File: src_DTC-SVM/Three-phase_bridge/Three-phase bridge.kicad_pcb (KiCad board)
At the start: 2 copper layers, 588 x 429.8 mm, 79 parts, among them K1 CONN_3, M1 MCP6022-I/P, M2 MCP6022-I/P, P1 CONN_1, P2 Fuse, P3 CONN_1, P4 CONN_1, P5 CONN_1, P6 CONN_2, SW1 SW_PUSH_SMALL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

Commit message: Kicad pcb has been separated into three bloks: stm32 connections, three-phase bridge and current sensing. The idea is to have the current operational and diffential amplifiers as close as possible to the shunt resistors and the stm32 pins so that there are no electromagnetic interferencies nor logs to the distance, specially because they are analog signals.
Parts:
- removed SW1, SW2, SW3, SW4, SW5, SW6: SW_PUSH_SMALL, SW_PUSH_SMALL
- moved STM32_CONN1 83.8 mm to (155.2, 56.4)
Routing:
- net VDD: track 205.6 -> 104.8 mm
- net N-0000029: track 12.6 -> 85.6 mm, vias 0 -> 1
- net N-0000031: track 0.00 -> 61.5 mm
- net N-000008: track 0.00 -> 61.3 mm
- net GND: track 432.6 -> 394.1 mm
- net N-000007: track 17.6 -> 28.2 mm, vias 0 -> 1
- net N-000005: track 16.9 -> 15.9 mm

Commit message: Updating the three parts of the pcb.
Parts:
- moved BT1 241.7 mm to (148.8, 124.0)
- moved BT2 241.7 mm to (148.8, 144.0)
- moved D1 241.7 mm to (144.3, 83.8)
- moved INA1 241.7 mm to (126.2, 46.7)
- moved INA2 241.7 mm to (126.0, 93.5)
- moved M1 241.7 mm to (126.0, 64.3)
- moved M2 241.7 mm to (128.5, 118.0)
- moved P2 241.7 mm to (143.8, 117.9)
- moved P6 241.7 mm to (148.8, 134.1)
- moved R10 241.7 mm to (119.6, 124.2)
- moved R6 241.7 mm to (124.7, 131.8)
- moved R8 241.7 mm to (119.6, 70.9)
- moved R9 241.7 mm to (134.6, 54.9)
- moved R_Shunt_2 241.7 mm to (117.3, 115.1)
- moved R11 241.7 mm to (129.8, 73.7)
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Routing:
- net GND: track 394.1 -> 328.2 mm

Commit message: Schematic and PCB updated.
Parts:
- added C10: 0.1uF, 6mm_C, F.Cu at (277.4, 105.4)
- added C11: 0.33uF, 6mm_C, F.Cu at (262.9, 108.0)
- added C12: 1000uF, 10mm_C, F.Cu at (411.0, 58.2)
- added C13: 1000uF, 10mm_C, F.Cu at (414.8, 79.8)
- added C14: 100uF, 6mm_C, F.Cu at (414.8, 88.9)
- added C15: 100uF, 6mm_C, F.Cu at (411.0, 67.8)
- added C8: 0.1uF, 6mm_C, F.Cu at (277.6, 18.0)
- added C9: 2.2uF, 6mm_C, F.Cu at (285.0, 15.5)
- C1, C2: footprint C1 -> 10mm_C
- C3, C4, C5, C6, C7: footprint C1 -> 6mm_C
- moved STM32_CONN1 189.4 mm to (210.1, 132.8)
- moved D1 185.0 mm to (329.2, 88.4)
- moved BT1 185.0 mm to (333.8, 128.5)
- moved BT2 185.0 mm to (333.8, 148.6)
- moved P2 185.0 mm to (328.7, 122.4)
- moved P6 185.0 mm to (333.8, 138.7)
- moved R_Shunt_2 161.0 mm to (273.1, 74.2), turned to 180 degrees
- moved R_Shunt_1 158.5 mm to (274.1, 42.2), turned to 180 degrees
- moved M2 105.1 mm to (230.0, 90.4)
- moved R10 105.1 mm to (221.1, 96.6)
- moved R12 105.1 mm to (223.6, 84.2)
- moved R6 101.5 mm to (221.1, 99.9), turned to 0 degrees
- moved R7 99.2 mm to (223.6, 80.9), turned to 0 degrees
- moved INA2 84.2 mm to (208.7, 77.6), turned to 180 degrees
- moved R9 79.7 mm to (208.9, 83.7)
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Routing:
- net N-0000064: track 144.1 -> 0.00 mm, vias 1 -> 0
- net +48V: track 25.5 -> 124.4 mm
- net GND: track 328.2 -> 421.1 mm
- net N-0000066: track 108.3 -> 20.9 mm
- net N-0000063: track 109.7 -> 23.9 mm, vias 1 -> 0
- net VCC: track 80.4 -> 161.1 mm
- net N-0000065: track 95.6 -> 20.5 mm
- net N-0000010: track 85.6 -> 12.2 mm, vias 1 -> 0
- net N-0000097: track 6.14 -> 71.1 mm, vias 0 -> 1
- net N-0000060: track 83.3 -> 19.8 mm
- net N-0000094: track 0.00 -> 59.2 mm
- net N-0000079: track 61.3 -> 2.54 mm
- net N-0000093: track 0.00 -> 55.1 mm
- net N-000007: track 61.5 -> 13.0 mm
- net N-0000068: track 54.1 -> 100.6 mm, vias 0 -> 1
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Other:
- board outline removed

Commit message: The two INA148 have been wired.
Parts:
- moved P5 123.2 mm to (342.9, 134.4)
- moved P4 93.6 mm to (241.3, 74.2)
- moved P1 86.8 mm to (248.4, 42.2)
- moved R6 68.0 mm to (214.4, 32.3), turned to 270 degrees
- moved R10 64.5 mm to (217.7, 32.3), turned to 270 degrees
- moved C14 62.9 mm to (360.7, 120.9)
- moved C13 62.7 mm to (360.7, 111.5)
- moved C12 60.9 mm to (360.7, 92.5)
- moved C15 60.9 mm to (360.7, 102.1)
- moved R12 49.8 mm to (230.1, 34.8), turned to 90 degrees
- moved M2 49.7 mm to (223.9, 41.1), turned to 90 degrees
- moved R7 47.1 mm to (233.4, 34.8), turned to 270 degrees
- moved INA1 45.4 mm to (236.0, 50.3), turned to 90 degrees
- moved R5 38.3 mm to (232.4, 71.9), turned to 270 degrees
- moved R8 37.8 mm to (218.7, 69.3), turned to 270 degrees
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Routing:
- net +3.3V: track 37.9 -> 166.0 mm, vias 2 -> 1
- net N-0000077: track 61.5 -> 120.8 mm
- net GND: track 421.1 -> 479.2 mm, vias 0 -> 2
- net N-0000097: track 71.1 -> 27.3 mm, vias 1 -> 0
- net N-00000101: track 17.3 -> 58.7 mm, vias 0 -> 1
- net VDD: track 105.9 -> 136.8 mm
- net N-0000010: track 12.2 -> 39.4 mm
- net N-0000075: track 6.78 -> 31.3 mm, vias 0 -> 1
- net N-0000084: track 89.7 -> 112.2 mm
- net N-000007: track 13.0 -> 27.6 mm
- net (no net): track 13.7 -> 0.00 mm
- net N-0000081: track 0.00 -> 10.8 mm
- net N-0000068: track 100.6 -> 109.4 mm
- net N-0000073: track 25.1 -> 32.1 mm
- net N-0000076: track 6.10 -> 12.4 mm
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
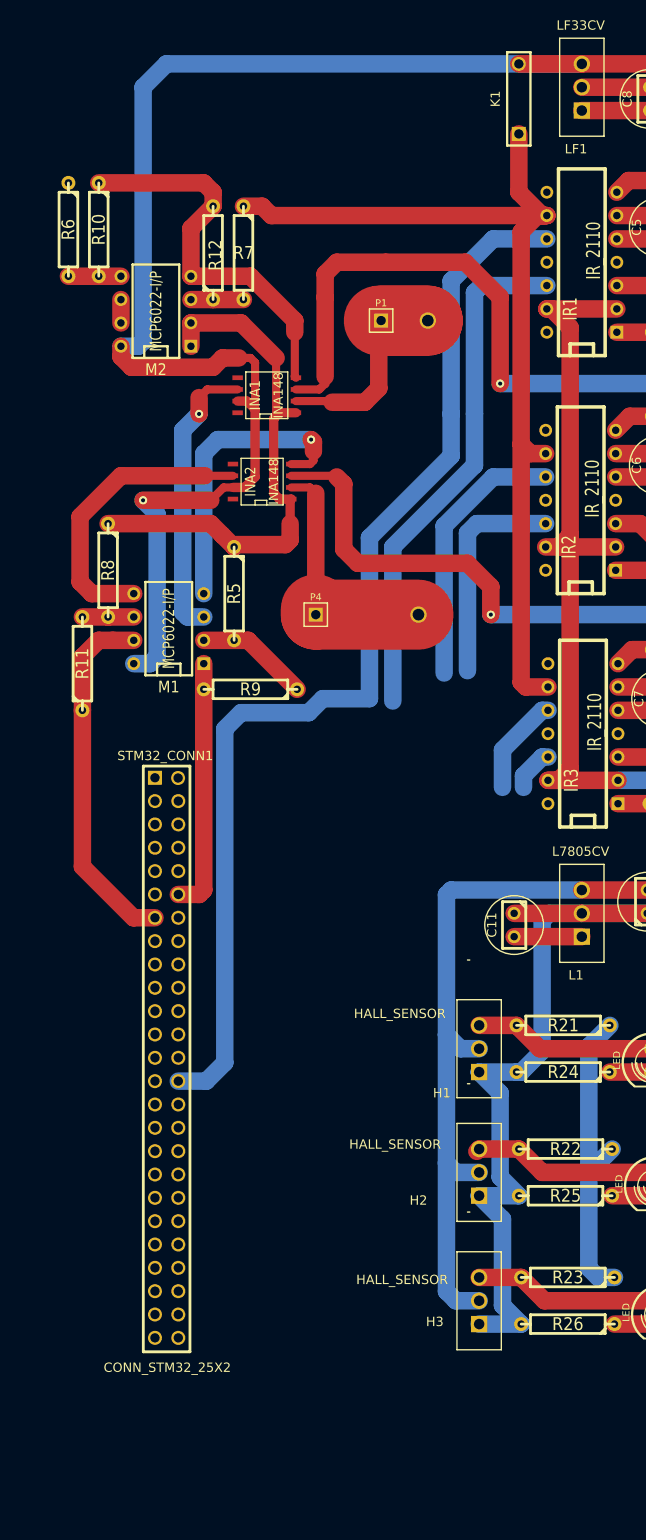
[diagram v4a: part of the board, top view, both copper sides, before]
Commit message: INA148s and MCP6s have been gotten closer.
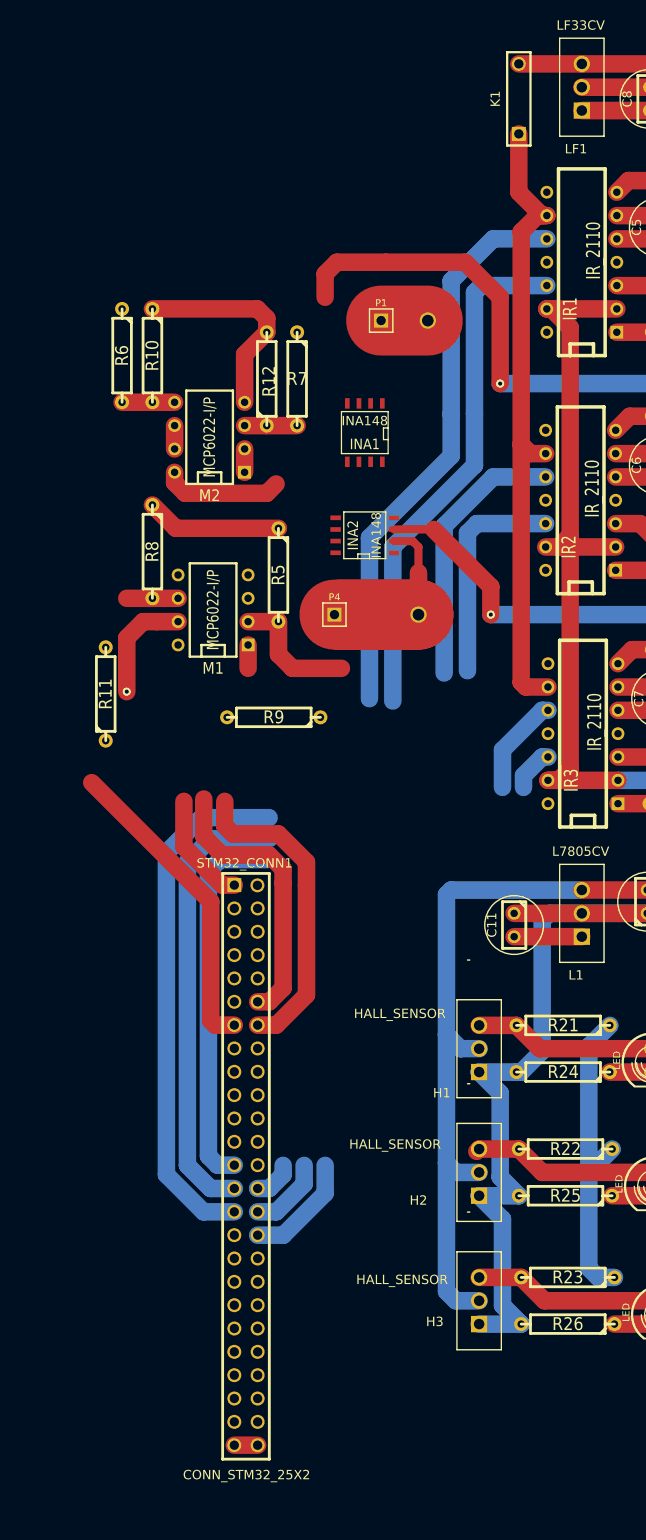
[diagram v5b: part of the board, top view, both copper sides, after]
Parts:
- moved R12 14.9 mm to (236.0, 48.5)
- moved R7 14.9 mm to (239.3, 48.5)
- moved R10 14.9 mm to (223.5, 46.0)
- moved M2 14.9 mm to (229.7, 54.9)
- moved R6 14.9 mm to (220.2, 46.0)
- moved STM32_CONN1 14.5 mm to (233.4, 131.8)
- moved INA2 12.6 mm to (246.6, 65.5)
- moved INA1 11.4 mm to (246.6, 54.4), turned to 180 degrees
- moved R8 5.24 mm to (223.5, 67.3)
- moved R5 5.24 mm to (237.2, 69.8)
- moved M1 5.24 mm to (230.1, 73.7)
- moved R11 4.17 mm to (218.4, 82.8)
- moved R9 3.97 mm to (236.7, 85.3)
- moved P4 2.03 mm to (243.3, 74.2)
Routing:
- net +3.3V: track 166.0 -> 34.7 mm, vias 1 -> 0
- net N-0000064: track 4.78 -> 61.6 mm
- net N-0000077: track 120.8 -> 65.9 mm
- net N-0000063: track 23.9 -> 73.0 mm
- net N-00000101: track 58.7 -> 17.3 mm
- net N-0000082: track 56.3 -> 97.4 mm
- net GND: track 479.2 -> 441.8 mm, vias 2 -> 1
- net N-0000079: track 2.54 -> 36.9 mm
- net VDD: track 136.8 -> 103.4 mm
- net N-0000073: track 32.1 -> 0.00 mm
- net N-0000075: track 31.3 -> 0.18 mm, vias 1 -> 0
- net N-0000062: track 27.5 -> 5.08 mm
- net N-0000068: track 109.4 -> 91.8 mm
- net N-0000084: track 112.2 -> 99.4 mm
- net N-0000081: track 10.8 -> 23.1 mm
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
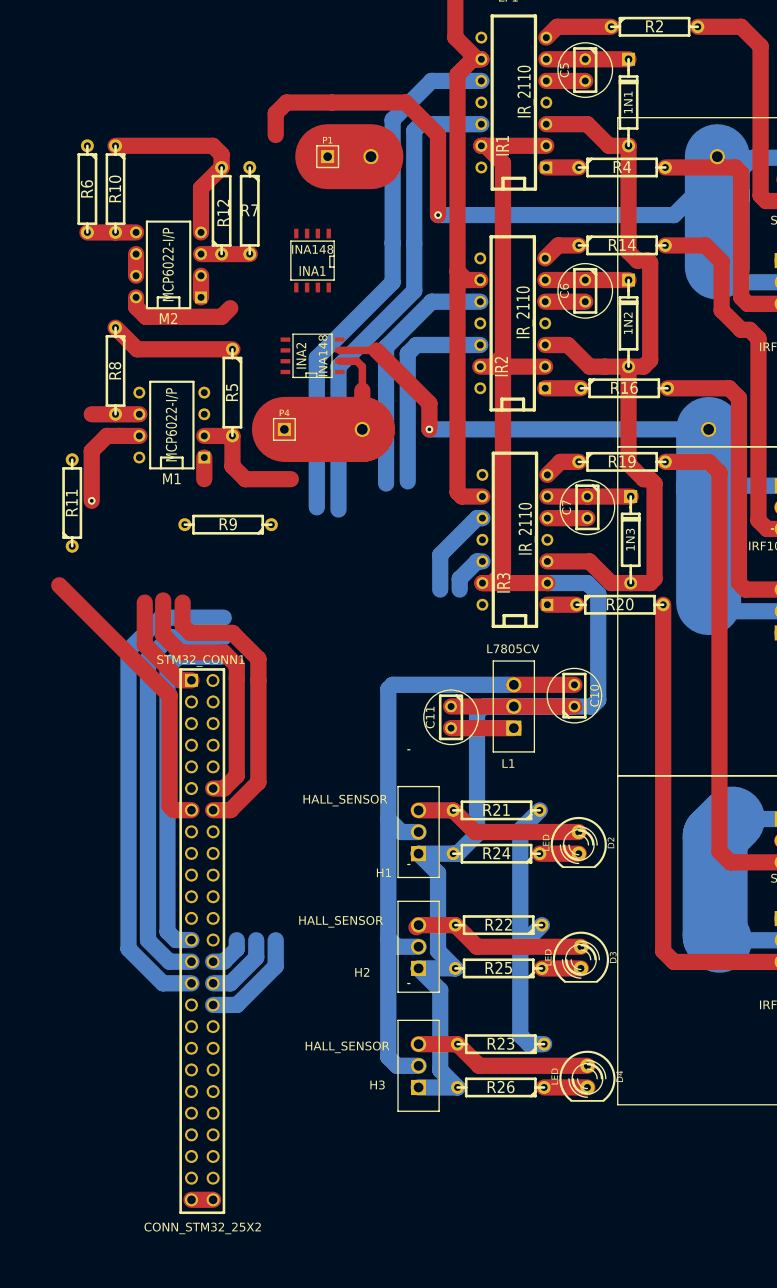
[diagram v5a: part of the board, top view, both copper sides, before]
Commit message: The conector from STM32 to the PCB has been fully wired up.
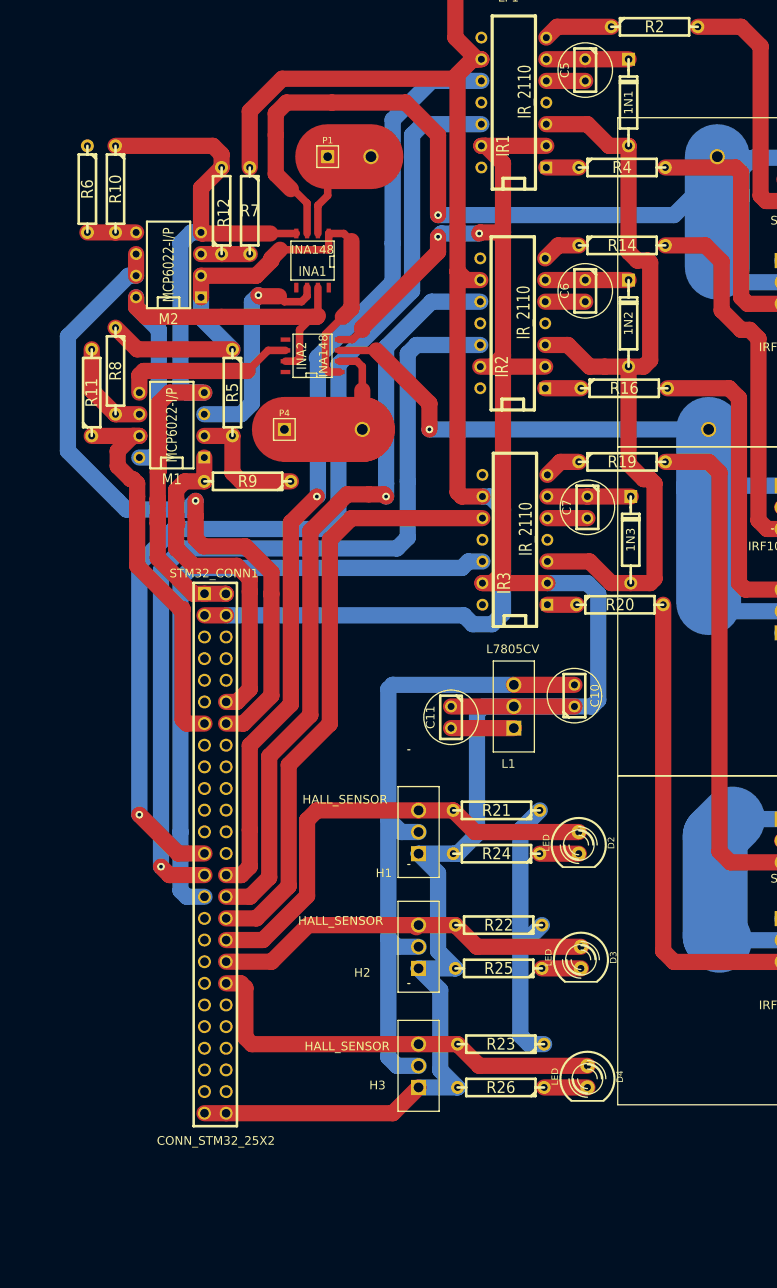
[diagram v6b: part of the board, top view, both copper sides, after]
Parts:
- moved R11 13.2 mm to (220.7, 69.8)
- moved STM32_CONN1 10.3 mm to (234.9, 121.7)
- moved R9 5.57 mm to (239.0, 80.3)
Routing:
- net GND: track 441.8 -> 548.5 mm, vias 1 -> 3
- net VDD: track 103.4 -> 189.9 mm
- net N-0000061: track 37.6 -> 90.2 mm, vias 1 -> 2
- net N-0000081: track 23.1 -> 70.5 mm
- net N-00000101: track 17.3 -> 64.3 mm
- net N-0000079: track 36.9 -> 81.3 mm, vias 0 -> 1
- net N-0000077: track 65.9 -> 110.2 mm, vias 0 -> 1
- net +3.3V: track 34.7 -> 76.9 mm
- net N-0000060: track 19.8 -> 53.9 mm
- net N-0000066: track 20.9 -> 49.8 mm
- net N-0000063: track 73.0 -> 101.4 mm, vias 0 -> 1
- net N-0000075: track 0.18 -> 26.8 mm, vias 0 -> 1
- net N-0000082: track 97.4 -> 121.9 mm, vias 0 -> 1
- net N-0000065: track 20.5 -> 44.8 mm
- net N-0000073: track 0.00 -> 20.4 mm
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
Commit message: The wire up for the Three-phase bridge has been completed. Nevertheless, the fillzones still remain undone.
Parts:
- removed K1: CONN_3, Battery_2x1
- removed P3: CONN_1, PIN_ARRAY_1
- added P7: CONN_1, PIN_ARRAY_1, F.Cu at (245.9, 141.7)
- added P8: CONN_1, PIN_ARRAY_1, F.Cu at (245.9, 144.8)
- added P9: CONN_1, PIN_ARRAY_1, F.Cu at (245.9, 147.8)
- P2: value Fuse -> POWER_FUSE
- P6: value CONN_2 -> POWER_FUSE; footprint PIN_ARRAY_2X1 -> Fuse
- S1, S2, S3, S4, S5, S6: footprint TO220_Big_Heat_Sink_no_copper -> TO220_Big_Heat_Sink
- moved C14 123.6 mm to (292.6, 17.8), turned to 90 degrees
- moved C13 110.6 mm to (302.0, 17.8), turned to 90 degrees
- moved C1 107.2 mm to (262.9, 99.6)
- moved C3 95.0 mm to (276.6, 98.8)
- moved C2 93.6 mm to (213.9, 34.0), turned to 90 degrees
- moved C4 86.9 mm to (214.1, 42.7)
- moved C12 84.2 mm to (309.1, 159.0), turned to 270 degrees
- moved C15 70.8 mm to (318.5, 159.0), turned to 270 degrees
- moved BT2 65.8 mm to (339.6, 83.1), turned to 90 degrees
- moved D1 62.5 mm to (341.9, 149.6), turned to 90 degrees
- moved P5 56.4 mm to (286.5, 136.4)
- moved P6 56.1 mm to (333.2, 82.5), turned to 0 degrees
- moved C8 49.3 mm to (230.9, 33.8)
- moved C9 49.3 mm to (238.3, 31.2)
- moved LF1 49.3 mm to (223.5, 32.5)
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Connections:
- BT1 pad 1: VCC -> N-0000067
- BT2 pad 1: +48V -> N-0000063
- C12 pad 1: VCC -> +48V
- C13 pad 1: VCC -> +48V
- C14 pad 1: VCC -> +48V
- C15 pad 1: VCC -> +48V
- P6 pad 2: VCC -> N-0000063
- R6 pad 1: VCC -> +48V
- STM32_CONN1 pad 40: (no net) -> N-0000064
- STM32_CONN1 pad 42: (no net) -> N-0000065
- STM32_CONN1 pad 44: (no net) -> N-0000066
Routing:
- net GND: track 548.5 -> 889.6 mm, vias 3 -> 7
- net +48V: track 124.4 -> 405.0 mm, vias 0 -> 1
- net VCC: track 161.1 -> 316.1 mm
- net N-0000010: track 28.5 -> 140.0 mm
- net N-0000077: track 91.8 -> 162.3 mm
- net N-0000069: track 112.6 -> 153.0 mm
- net +3.3V: track 76.9 -> 103.9 mm
- net VDD: track 189.9 -> 216.5 mm, vias 0 -> 1
- net N-0000089: track 28.9 -> 18.2 mm
- net N-0000066: track 0.00 -> 9.81 mm
- net N-0000065: track 0.00 -> 9.60 mm
- net N-0000064: track 0.00 -> 9.39 mm
- net N-0000063: track 0.00 -> 6.37 mm
- net N-0000067: track 0.00 -> 5.65 mm
- net N-0000093: track 55.1 -> 49.9 mm
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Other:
- board outline added: 474 x 429 mm

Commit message: A couple of capacitors have been added to VDD, and a LED for the 48V signal (just for having a visual check).
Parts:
- added C16: 10uF, 6mm_C, F.Cu at (182.1, 75.9)
- added C17: 100uF, 6mm_C, F.Cu at (174.2, 75.9)
- added D5: LED, LED-5MM, F.Cu at (224.8, 206.2)
- moved RGL3 87.7 mm to (258.3, 93.2)
- moved R17 87.7 mm to (268.9, 90.9)
- moved RGL1 87.7 mm to (258.3, 79.5)
- moved RGL2 87.7 mm to (258.3, 86.1)
- moved 1N1 87.7 mm to (209.8, 83.1)
- moved 1N2 87.7 mm to (209.8, 109.0)
- moved C14 87.7 mm to (218.7, 65.0)
- moved C15 87.7 mm to (244.6, 206.2)
- moved C4 87.7 mm to (140.2, 89.9)
- moved C9 87.7 mm to (164.3, 78.5)
- moved IR2 87.7 mm to (196.2, 109.0)
- moved LF1 87.7 mm to (149.6, 79.8)
- moved P1 87.7 mm to (174.5, 89.4)
- moved P7 87.7 mm to (172.0, 189.0)
- moved P8 87.7 mm to (172.0, 192.0)
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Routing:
- net GND: track 889.6 -> 922.4 mm
- net +48V: track 405.0 -> 415.4 mm
- net VDD: track 216.5 -> 226.7 mm
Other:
- board size 474 x 429 mm -> 400.1 x 429 mm
